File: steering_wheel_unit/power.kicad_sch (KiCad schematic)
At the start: 23 parts, among them IC2 LM76202QPWPRQ1, U4 TPS62933

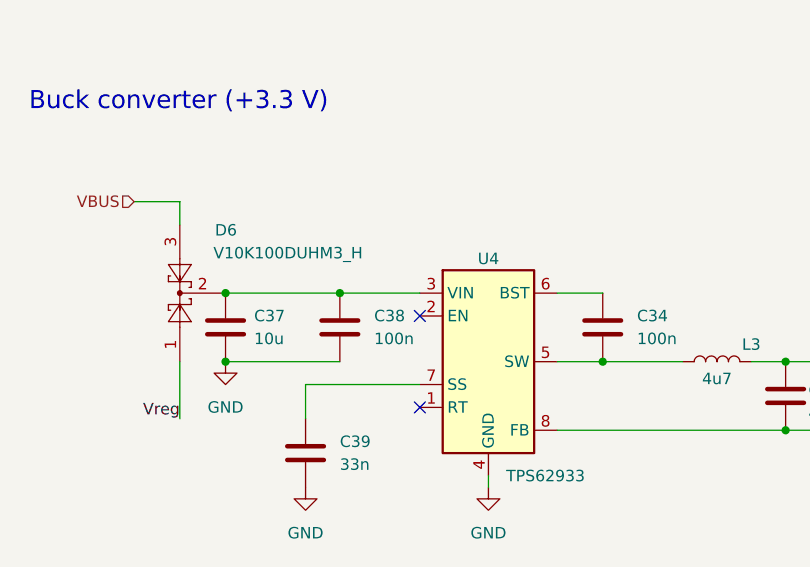
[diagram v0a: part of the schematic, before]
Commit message: Add zones for gnd and power
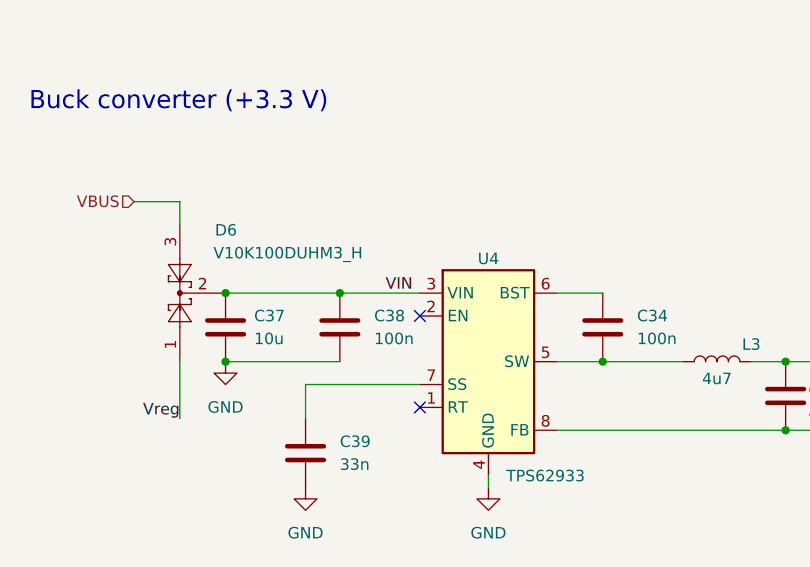
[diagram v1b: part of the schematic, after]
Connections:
- net VIN: now reaches C37.1, C38.1, D6.2, U4.3 (VIN)
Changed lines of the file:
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@@
+		)
+	)
+	(label "VIN"
+		(at 184.15 44.45 0)
+		(effects
+			(font
+				(size 1.27 1.27)
+			)
+			(justify left bottom)
 		)
 	)

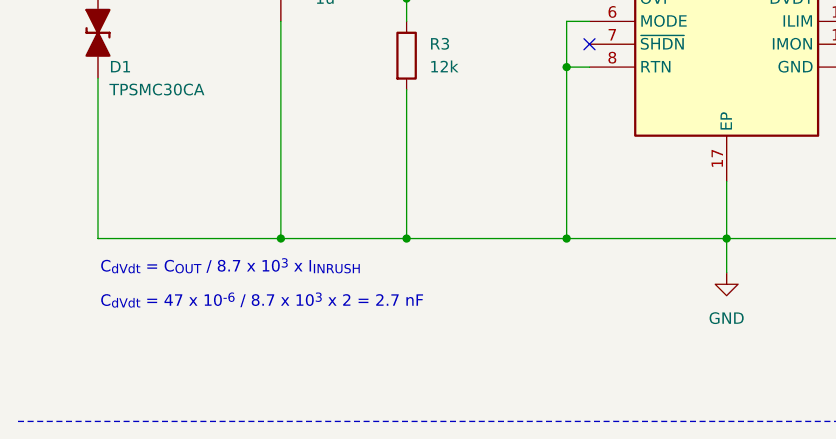
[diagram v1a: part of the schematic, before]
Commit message: Add dimensions
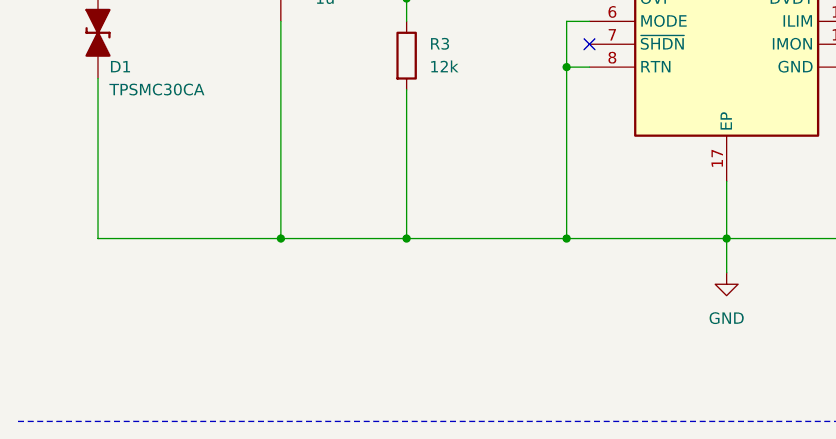
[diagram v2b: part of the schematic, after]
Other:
- note removed: "C_{dVdt} = 47 x 10^{-6} / 8.7 x 10^{3} x 2 = 2.7 nF"
- note removed: "C_{dVdt} = C_{OUT} / 8.7 x 10^{3} x I_{INRUSH}"
- title: (none) -> Steering_wheel_unit_pwr
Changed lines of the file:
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@@
 	(generator_version "9.0")
 	(paper "A4")
-	(text "C_{dVdt} = C_{OUT} / 8.7 x 10^{3} x I_{INRUSH}"
-		(exclude_from_sim no)
-		(at 21.844 76.454 0)
-		(effects
-			(font
-				(size 1.27 1.27)
-			)
-			(justify left bottom)
-		)
-	)
-	(text "C_{dVdt} = 47 x 10^{-6} / 8.7 x 10^{3} x 2 = 2.7 nF"
-		(exclude_from_sim no)
-		(at 21.844 80.264 0)
-		(effects
-			(font
-				(size 1.27 1.27)
-			)
-			(justify left bottom)
-		)
+	(title_block
+		(title "Steering_wheel_unit_pwr")
+		(date "2025-03-22")
 	)
 	(text "Ideal diode circuit\n"

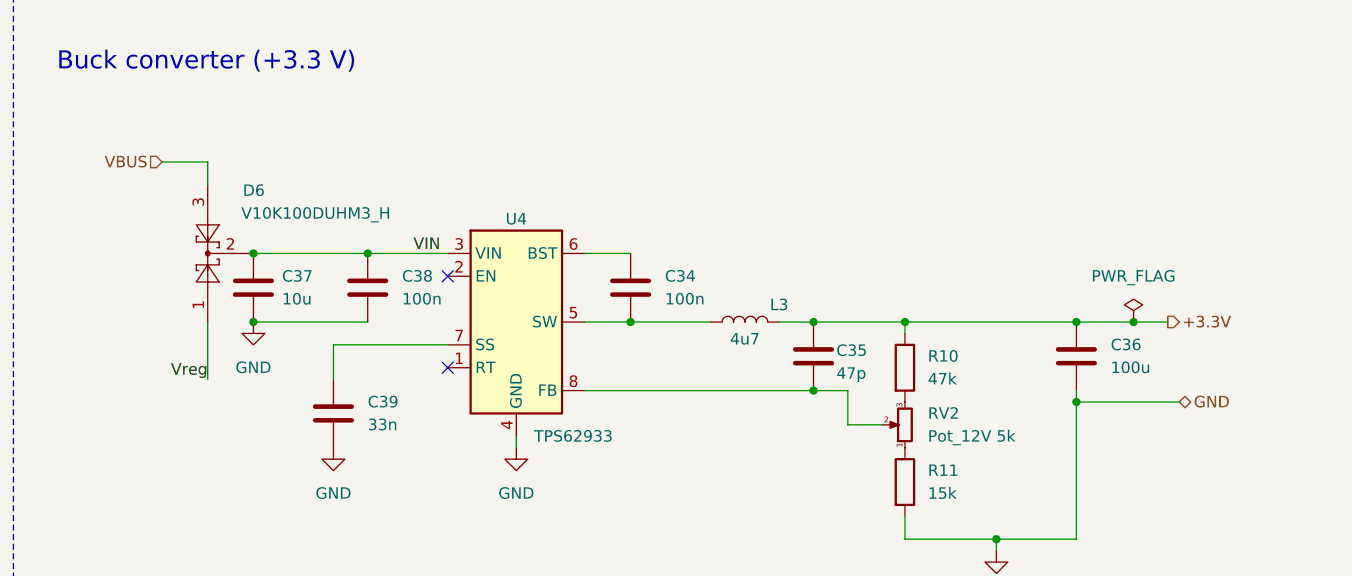
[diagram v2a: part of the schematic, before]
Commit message: Add no GND zones and logo
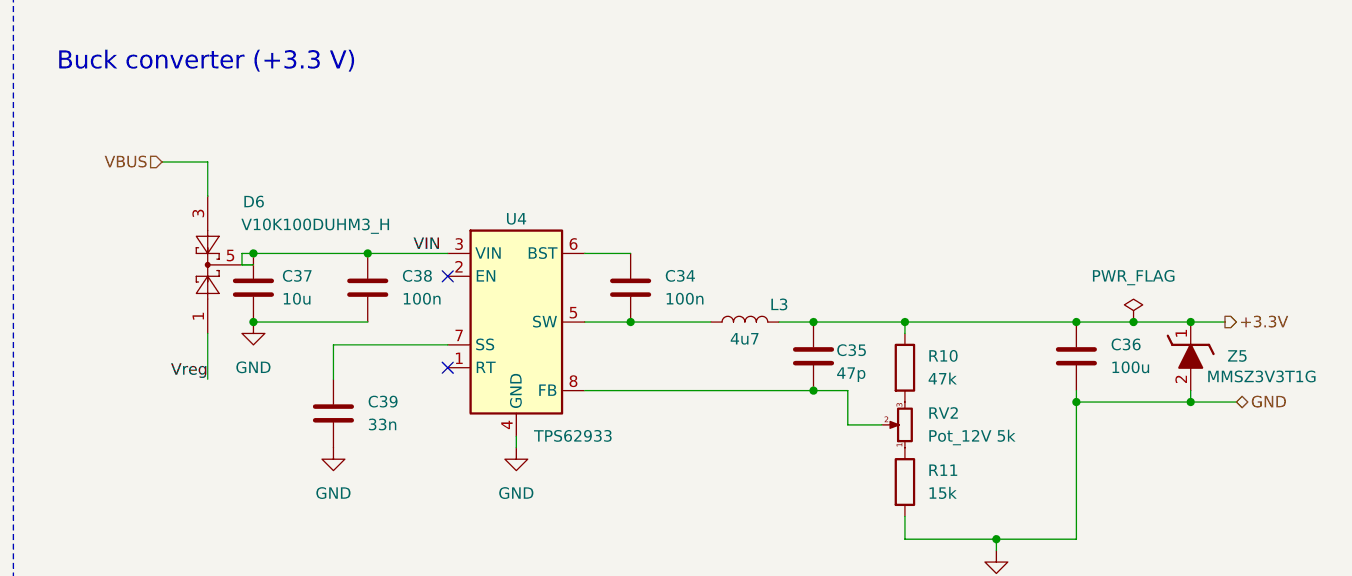
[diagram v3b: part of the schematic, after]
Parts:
- added Z5: MMSZ3V3T1G, Lib:SOD3716X135N, symbol Zener 3.3V:MMSZ3V3T1G
- D6: footprint Lib:DPAK228P990X239-4N -> Lib:V10K100DUHM3H
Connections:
- net +3.3V: now also Z5.1 (K)
- net GND: now also Z5.2 (A)
- net VBUS: now also D6.4
- net VIN: now also D6.5, D6.6, D6.7, D6.8; no longer D6.2
- net Vreg: now also D6.2

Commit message: Add manufacturing
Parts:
- renumbered Z5 to Z3
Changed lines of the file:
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@@
 		(on_board yes)
 		(dnp no)
-		(property "Reference" "Z5"
+		(property "Reference" "Z3"
 			(at 274.574 55.88 90)
 			(effects
@@
 			(project "steering_wheel_unit"
 				(path "/b435671d-bfd7-4707-b36e-3eecb7fa1f89/61ddc585-00ca-4289-9fa8-971703329eaa"
-					(reference "Z5")
+					(reference "Z3")
 					(unit 1)
 				)
